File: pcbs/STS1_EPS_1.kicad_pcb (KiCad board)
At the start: 4 copper layers, 81 x 85 mm, 120 parts, among them J1 Inter-EPS, J2 Panel X+, J3 Battery Pack, J4 Panel X-, J5 Panel Y+, J6 Panel Y-, J7 Panel Z+, Q1 SI7135DP-T1-GE3, U1 LTC4020EUHFPBF, U10 MAX11632EEGT, U11 TMCS1101A3B-Q1, U12 BD50GA5WEFJ, U13 TMCS1101A3B-Q1, U14 LM334M, U15 LM334M, U16 LM334M, U17 LM334M, U18 LM334M, U19 TMCS1101A3B-Q1, U2 SI7272DP-T1-GE3, U20 TMCS1101A3B-Q1, U21 TMCS1101A3B-Q1, U22 TMCS1101A3B-Q1, U23 TMCS1101A3B-Q1, U24 TMCS1101A3B-Q1, U25 TMCS1101A3B-Q1, U26 TMCS1101A3B-Q1, U3 SI7272DP-T1-GE3, U4 BQ29209DRBT, U5 MAX11632EEGT, U6 MAX11632EEGT, U7 MAX11632EEGT, U8 MAX11632EEGT, U9 MAX11632EEGT

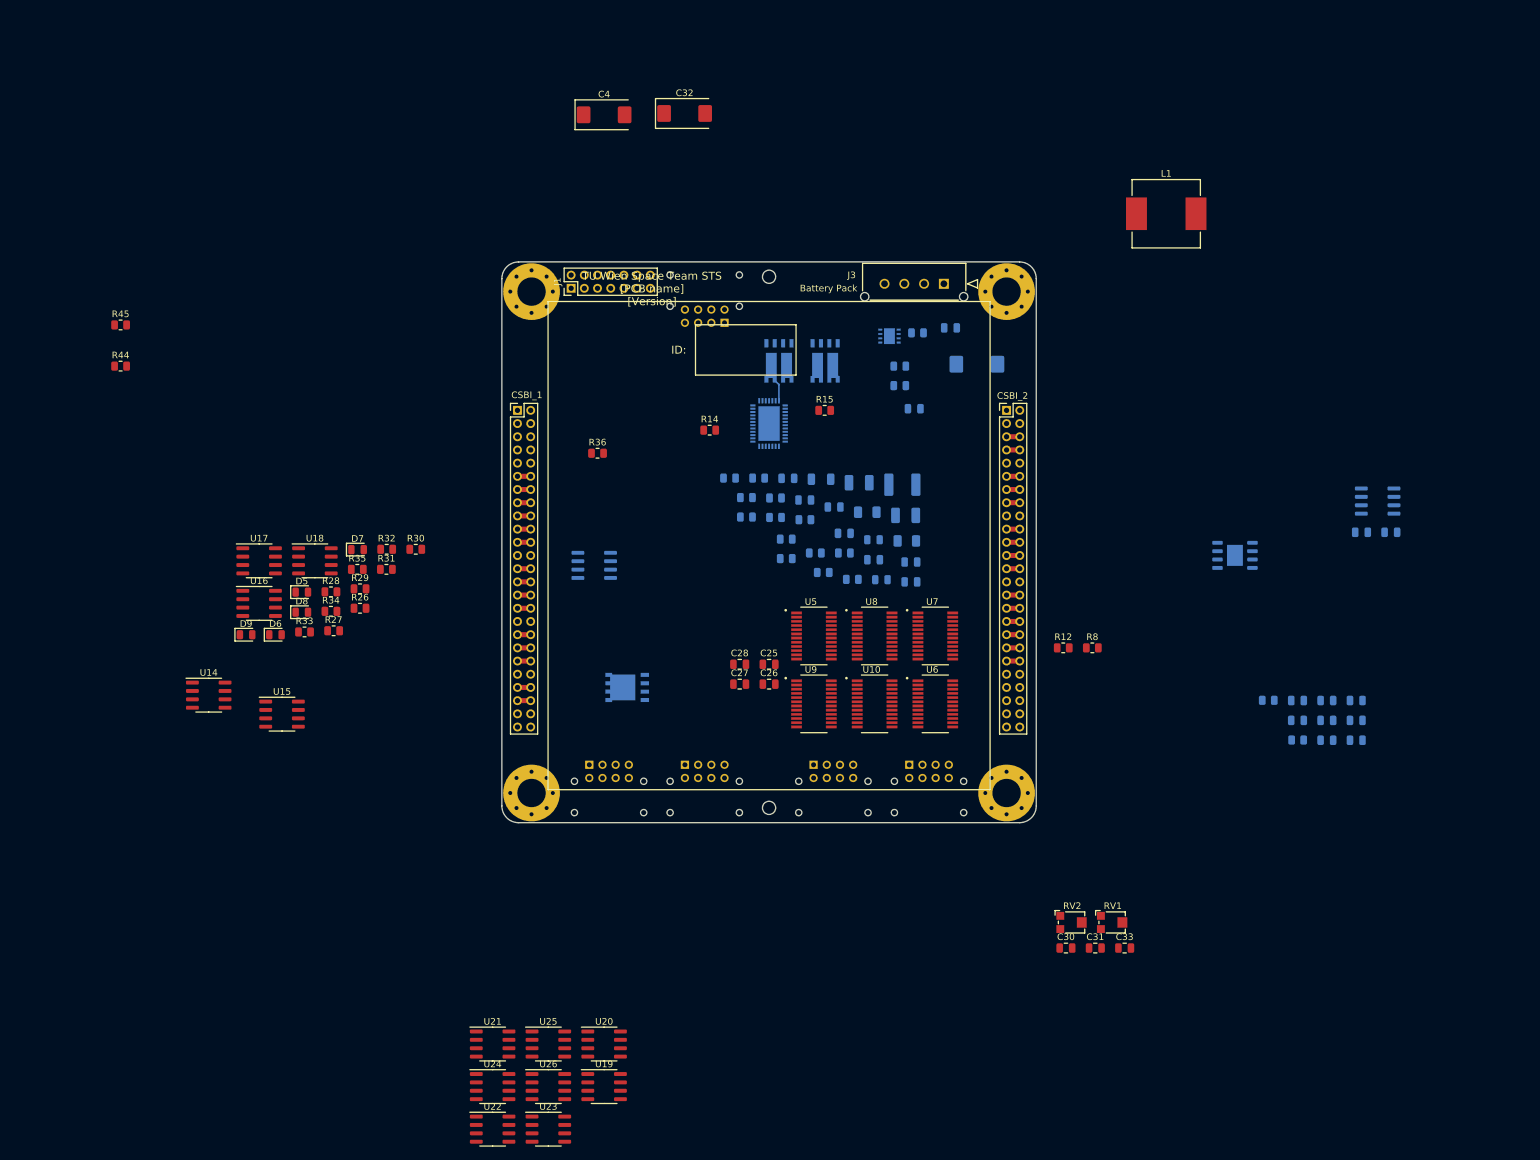
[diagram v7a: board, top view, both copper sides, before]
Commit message: Worked on STS1_EPS_2 layout.
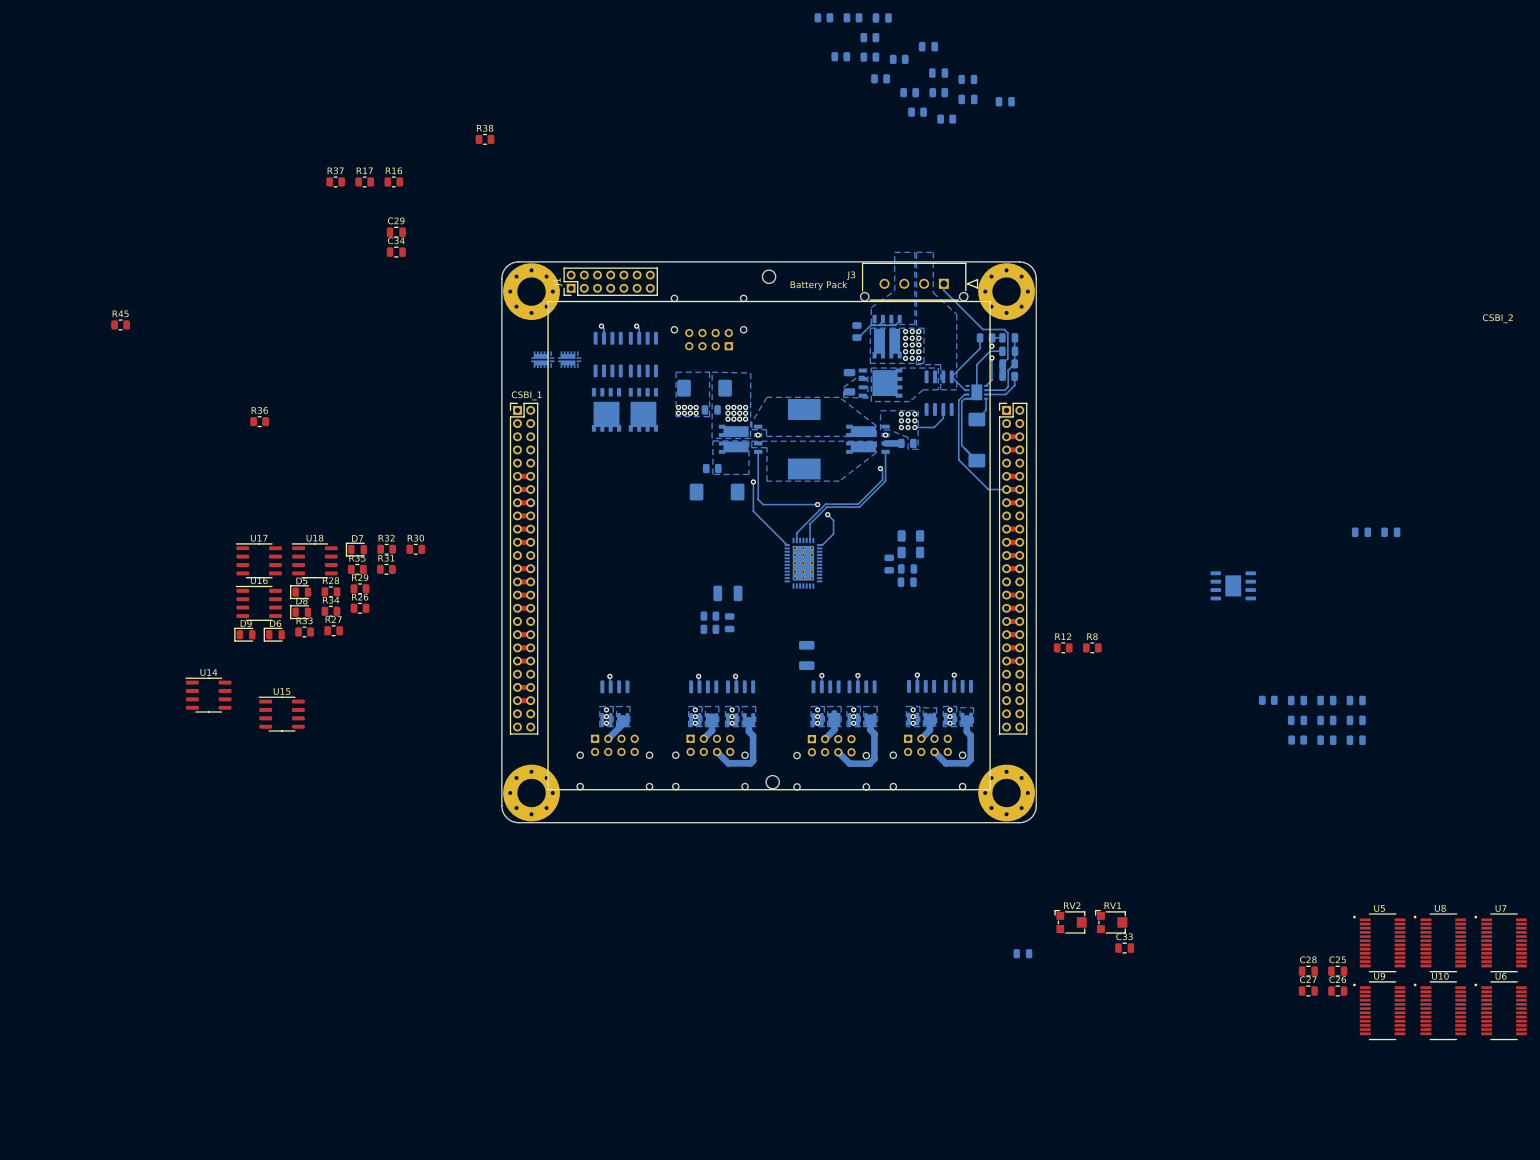
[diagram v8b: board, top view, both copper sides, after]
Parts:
- removed R44: 0, Resistor_SMD:R_0805_2012Metric
- added C29: 100n, Capacitor_SMD:C_0805_2012Metric, F.Cu at (100.1, 37.3)
- added C34: 100n, Capacitor_SMD:C_0805_2012Metric, F.Cu at (100.1, 40.3)
- added Q2: SI7135DP-T1-GE3, STS_Package_SO:POWERPAK_SO8_single, B.Cu at (132.0, 64.2)
- added Q3: SI7135DP-T1-GE3, STS_Package_SO:POWERPAK_SO8_single, B.Cu at (137.6, 64.2)
- added Q4: SI7272DP-T1-GE3, STS_Package_SO:POWERPAK_SO8, B.Cu at (174.5, 50.1)
- added R16: 100k, Resistor_SMD:R_0805_2012Metric, F.Cu at (99.8, 29.7)
- added R17: 100k, Resistor_SMD:R_0805_2012Metric, F.Cu at (95.3, 29.7)
- added R37: 0, Resistor_SMD:R_0805_2012Metric, F.Cu at (90.9, 29.7)
- added R38: 100k, Resistor_SMD:R_0805_2012Metric, F.Cu at (113.6, 23.2)
- added R39: 1M, Resistor_SMD:R_0805_2012Metric, B.Cu at (170.0, 52.4)
- added U27: LTC4451AV#TRMPBF, STS_Package_DFN_QFN:AD_LQFN-16, B.Cu at (126.4, 56.6)
- added U28: LTC4451AV#TRMPBF, STS_Package_DFN_QFN:AD_LQFN-16, B.Cu at (122.3, 56.6)
- C30, C31, C32, C4, L1, R14, R15, U19, U20, U21, U22, U23, U24, U25, U26: moved to B.Cu
- C8: footprint Capacitor_SMD:C_1812_4532Metric -> Capacitor_SMD:C_0805_2012Metric
- R36: value R -> 100k
- moved U11 118.7 mm to (132.2, 55.9), turned to 90 degrees
- moved U24 113.3 mm to (137.6, 55.9), turned to 90 degrees
- moved C31 100.2 mm to (147.9, 64.2)
- moved C27 97.9 mm to (238.4, 152.3)
- moved C28 97.9 mm to (238.4, 149.3)
- moved U5 97.9 mm to (249.6, 145.0)
- moved U9 97.9 mm to (249.6, 155.3)
- moved C25 97.9 mm to (242.8, 149.3)
- moved C26 97.9 mm to (242.8, 152.3)
- moved U10 97.9 mm to (258.8, 155.3)
- moved U6 97.9 mm to (268.0, 155.3)
- moved U7 97.9 mm to (268.0, 145.0)
- moved U8 97.9 mm to (258.8, 145.0)
- moved U26 85.1 mm to (185.3, 108.6), turned to 90 degrees
- moved U25 76.7 mm to (179.7, 108.6), turned to 90 degrees
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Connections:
- C30 pad 2: /DS1_L -> /MPPT_BUS
- C31 pad 2: /BCC_OUT -> /Battery Charge Controller/VOUT
- C32 pad 1: /BCC_OUT -> /Battery Charge Controller/VOUT
- C4 pad 1: /DS1_L -> /MPPT_BUS
- CSBI_2 pad 13: unconnected-(CSBI_2-Pad13) -> /BAT_FAULT
- CSBI_2 pad 14: unconnected-(CSBI_2-Pad13) -> /BAT_FAULT
- D3 pad 2: /BCC_OUT -> /Battery Charge Controller/VOUT
- D4 pad 2: /BCC_OUT -> /Battery Charge Controller/VOUT
- J1 pad 1: /DS1_H -> /INTERNAL_V
- J1 pad 10: unconnected-(J1-Pad10) -> /DS2_SIGNAL_1
- J1 pad 11: unconnected-(J1-Pad11) -> GND
- J1 pad 12: unconnected-(J1-Pad12) -> /DS4_SIGNAL_1
- J1 pad 13: unconnected-(J1-Pad13) -> GND
- J1 pad 14: unconnected-(J1-Pad14) -> GND
- J1 pad 3: /DS1_L -> /INTERNAL_V
- J1 pad 5: unconnected-(J1-Pad5) -> /INTERNAL_V
- J1 pad 6: unconnected-(J1-Pad6) -> /BATT_RAW
- J1 pad 7: unconnected-(J1-Pad7) -> /INTERNAL_V
- J1 pad 8: unconnected-(J1-Pad8) -> /VOUT_I
- J1 pad 9: unconnected-(J1-Pad9) -> /DS1_SIGNAL_1
- J3 pad 1: /BATT_RAW -> /CENTER
- J3 pad 2: GNDREF -> /BATT_RAW
- J3 pad 3: /NTC -> GNDREF
- J3 pad 4: /CENTER -> /Battery/NTC
- R12 pad 1: /DS1_L -> /MPPT_BUS
- R15 pad 1: /DS1_L -> /MPPT_BUS
- R18 pad 1: /BCC_OUT -> /Battery Charge Controller/VOUT
- R20 pad 2: /BCC_OUT -> /Battery Charge Controller/VOUT
- R22 pad 1: /Battery Charge Controller/BATT -> /BATT_RAW
- R45 pad 1: /DS1_H -> Net-(Q2-Pad1)
- R45 pad 2: /DS1_L -> Net-(Q2-Pad5)
- R8 pad 1: /DS1_L -> /MPPT_BUS
- U1 pad 13: /Battery Charge Controller/STAT2 -> /BAT_FAULT
- U1 pad 16: /NTC -> /Battery/NTC
- U1 pad 36: /DS1_L -> /MPPT_BUS
- U1 pad 7: /DS1_L -> /MPPT_BUS
- U11 pad 3: /DS1_H -> Net-(Q2-Pad1)
- U11 pad 4: /DS1_H -> Net-(Q2-Pad1)
- U2 pad 1: /Battery Charge Controller/SW1 -> /Battery Charge Controller/SW2
- U2 pad 10: /BCC_OUT -> /Battery Charge Controller/SENSTOP
- U2 pad 11: /Battery Charge Controller/SENSTOP -> /Battery Charge Controller/VOUT
- U2 pad 12: /BCC_OUT -> /Battery Charge Controller/SENSTOP
- U2 pad 2: /Battery Charge Controller/TG1 -> /Battery Charge Controller/TG2
- U2 pad 3: /Battery Charge Controller/SW2 -> /Battery Charge Controller/SW1
- U2 pad 4: /Battery Charge Controller/TG2 -> /Battery Charge Controller/TG1
- U2 pad 5: /BCC_OUT -> /Battery Charge Controller/SENSTOP
- U2 pad 6: /BCC_OUT -> /Battery Charge Controller/SENSTOP
- U2 pad 7: /Battery Charge Controller/SENSTOP -> /Battery Charge Controller/VOUT
- U2 pad 8: /Battery Charge Controller/SENSTOP -> /Battery Charge Controller/VOUT
- U2 pad 9: /Battery Charge Controller/SENSTOP -> /Battery Charge Controller/VOUT
- U3 pad 1: /Battery Charge Controller/SENSBOT -> GND
- U3 pad 10: /Battery Charge Controller/SW2 -> /Battery Charge Controller/SW1
- U3 pad 11: /Battery Charge Controller/SW1 -> /Battery Charge Controller/SW2
- U3 pad 12: /Battery Charge Controller/SW2 -> /Battery Charge Controller/SW1
- U3 pad 2: /Battery Charge Controller/BG1 -> /Battery Charge Controller/BG2
- U3 pad 3: GND -> /Battery Charge Controller/SENSBOT
- U3 pad 4: /Battery Charge Controller/BG2 -> /Battery Charge Controller/BG1
- U3 pad 5: /Battery Charge Controller/SW2 -> /Battery Charge Controller/SW1
- U3 pad 6: /Battery Charge Controller/SW2 -> /Battery Charge Controller/SW1
- U3 pad 7: /Battery Charge Controller/SW1 -> /Battery Charge Controller/SW2
- U3 pad 8: /Battery Charge Controller/SW1 -> /Battery Charge Controller/SW2
- U3 pad 9: /Battery Charge Controller/SW1 -> /Battery Charge Controller/SW2
- U7 pad 10: /DS1_L -> /MPPT_BUS
- U9 pad 10: /DS1_L -> /MPPT_BUS
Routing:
- net /MPPT Bus Junction/MPPT_SUM: track 0.00 -> 96.2 mm, vias 0 -> 21
- net /Battery Charge Controller/BG2: track 0.00 -> 25.0 mm, vias 0 -> 2
- net /Battery Charge Controller/TG1: track 0.00 -> 24.8 mm, vias 0 -> 2
- net GNDREF: track 0.00 -> 24.2 mm
- net GND: track 0.00 -> 22.0 mm, vias 0 -> 41
- net /BAT_FAULT: track 0.00 -> 21.8 mm
- net /Battery Charge Controller/BG1: track 0.00 -> 21.1 mm
- net /CENTER: track 0.00 -> 20.3 mm
- net /Battery Charge Controller/TG2: track 0.00 -> 19.1 mm, vias 0 -> 2
- net /Panel_X+_6: track 0.00 -> 13.2 mm
- net /Panel_Z+_6: track 0.00 -> 12.9 mm
- net /Panel_X-_6: track 0.00 -> 12.8 mm
- net /Battery/VC1: track 0.00 -> 11.4 mm
- net /BATT_RAW: track 0.00 -> 10.9 mm
- net /Battery/VC2: track 0.00 -> 9.22 mm, vias 0 -> 2
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- added copper zone on B.Cu, net /BATT_RAW
- added copper zone on B.Cu, net /Battery Charge Controller/BATT
- added copper zone on B.Cu, net /Battery Charge Controller/SENSTOP
- added copper zone on B.Cu, net /Battery Charge Controller/SW1
- added copper zone on B.Cu, net /Battery Charge Controller/SW2
- added copper zone on B.Cu, net /Battery Charge Controller/VOUT
- added copper zone on In2.Cu, net /Battery Charge Controller/VOUT
- added copper zone on B.Cu, net /MPPT Bus Junction/MPPT_SUM
- added copper zone on B.Cu, net /Panel_X+_6
- added copper zone on B.Cu, net /Panel_X-_3
- added copper zone on B.Cu, net /Panel_X-_6
- added copper zone on B.Cu, net /Panel_Y+_3
- added copper zone on B.Cu, net /Panel_Z+_3
- added copper zone on B.Cu, net /Panel_Z+_6
- added copper zone on B.Cu, net GND
- added copper zone on B.Cu, net GNDREF
- added copper zone on B.Cu, net Net-(Q1-Pad1)
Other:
- outline, holes or cut-outs redrawn
- board text removed: "ID:"
- board text removed: "TU Wien Space Team STS [PCB name] [Version]"
